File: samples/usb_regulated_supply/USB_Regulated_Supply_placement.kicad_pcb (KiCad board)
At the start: 2 copper layers, 50 x 70 mm, 3 parts, among them J1 USB-C, U1 AP62300, U2 TLV75518

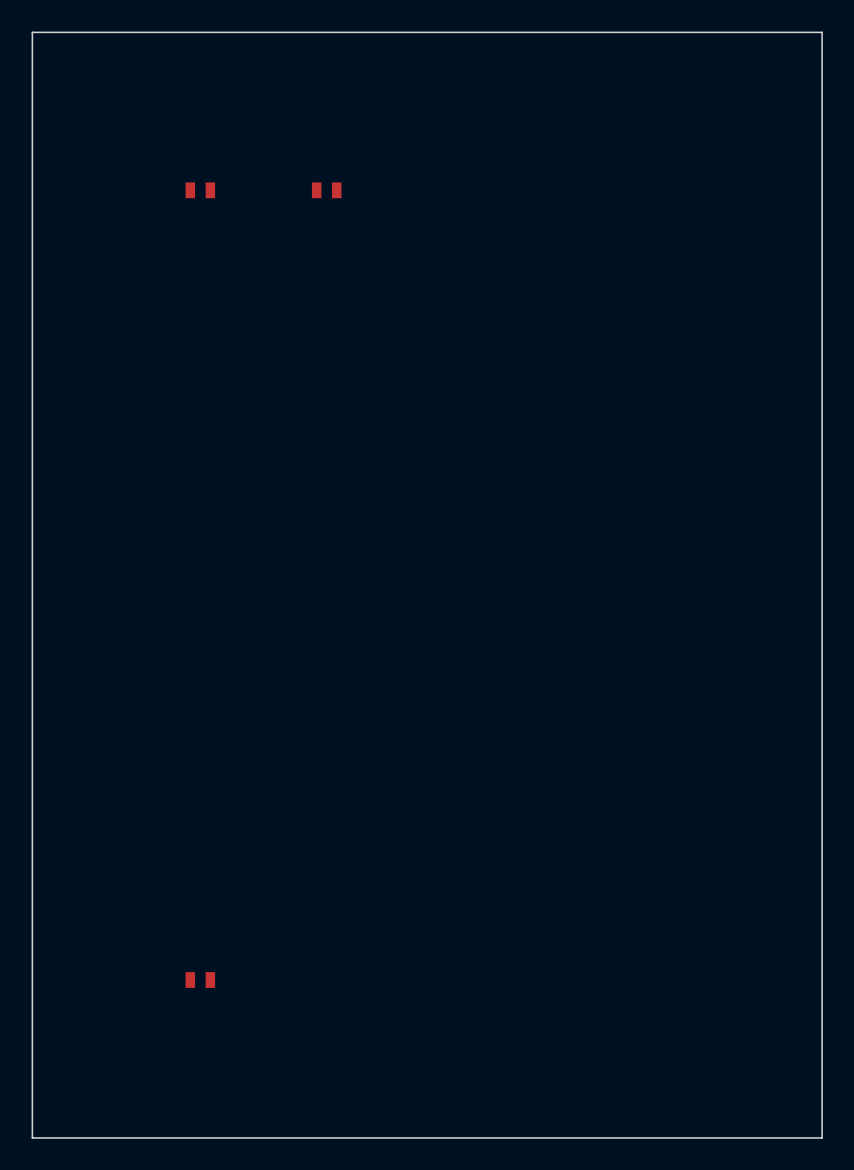
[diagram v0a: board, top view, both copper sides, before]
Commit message: chore: regenerate 8 sample designs against v0.27.0 engine
All 8 samples pass full validation (0 ERC errors):
- led_power_indicator, iot_sensor_node, usb_regulated_supply,
  usb_uart_bridge, oled_display_module, battery_iot_sensor,
  motor_controller, fpga_power_carrier

New artifacts per sample: .kicad_sch, _test_points.csv, _pinout.csv,
canonical_spec.yaml, design_ir.json, validation_report.json; MCU samples
also emit sdkconfig.defaults / .ioc stubs.

Also adds samples/*/svg/ to .gitignore — schematic SVG exports are
regenerable and too large to track.

zigbee_humidistat deferred: non-deterministic schematic output across
two generation runs (text annotation ordering vs sheet_instances).
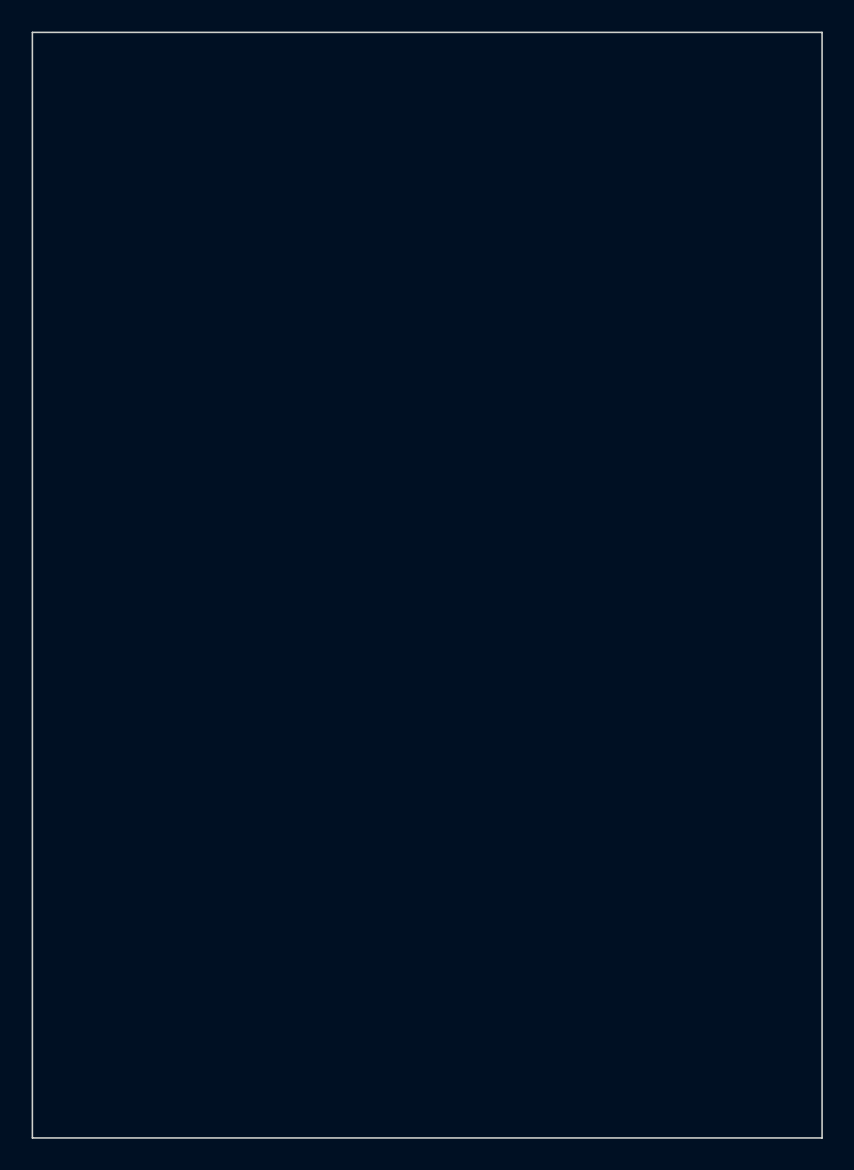
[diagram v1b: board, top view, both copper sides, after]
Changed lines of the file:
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@@
-(kicad_pcb (version 20240108) (generator "schematic_engine")
+(kicad_pcb (version 20240108) (generator "schematic_engine placement_preview")
   (general (thickness 1.6) (legacy_teardrops no))
   (layers
@@
       (effects (font (size 1.0 1.0) (thickness 0.15)))
     )
-    (pad "1" smd rect (at 0.00 0) (size 0.6 1.0) (layers "F.Cu" "F.Paste" "F.Mask") (net 7 "VBUS_5V"))
-    (pad "2" smd rect (at 1.27 0) (size 0.6 1.0) (layers "F.Cu" "F.Paste" "F.Mask") (net 3 "GND"))
   )
   (footprint "SOT-23-5"
@@
       (effects (font (size 1.0 1.0) (thickness 0.15)))
     )
-    (pad "1" smd rect (at 0.00 0) (size 0.6 1.0) (layers "F.Cu" "F.Paste" "F.Mask") (net 9 "VDD_3P3"))
-    (pad "2" smd rect (at 1.27 0) (size 0.6 1.0) (layers "F.Cu" "F.Paste" "F.Mask") (net 3 "GND"))
   )
   (footprint "Connector_USB:USB_C_Receptacle_GCT_USB4085"
@@
       (effects (font (size 1.0 1.0) (thickness 0.15)))
     )
-    (pad "1" smd rect (at 0.00 0) (size 0.6 1.0) (layers "F.Cu" "F.Paste" "F.Mask") (net 7 "VBUS_5V"))
-    (pad "2" smd rect (at 1.27 0) (size 0.6 1.0) (layers "F.Cu" "F.Paste" "F.Mask") (net 3 "GND"))
   )
   (gr_line (start 0.00 0.00) (end 50.00 0.00) (stroke (width 0.1) (type solid)) (layer "Edge.Cuts"))
